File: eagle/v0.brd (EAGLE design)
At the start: 85.9 x 43.9 mm, 50 parts, among them IC1 MCP23008/SO, J12 455-1750-1-ND, J13 455-1750-1-ND, J14 455-1750-1-ND, J15 455-1750-1-ND, Q1 IRLML6244, Q2 IRLML6244, Q3 IRLML6244, Q4 IRLML6244, Q5 IRLML6244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

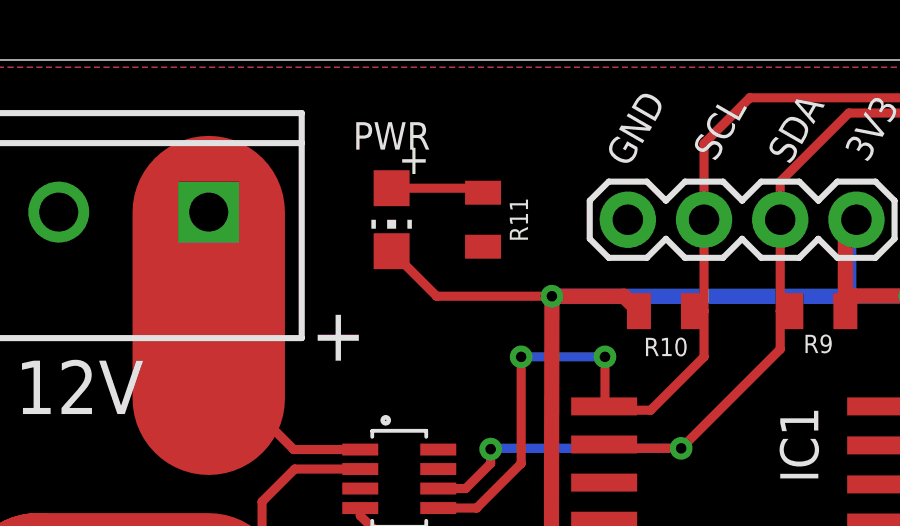
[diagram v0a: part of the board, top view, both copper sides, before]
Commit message: Fix LED polarity - caught by my dad :)
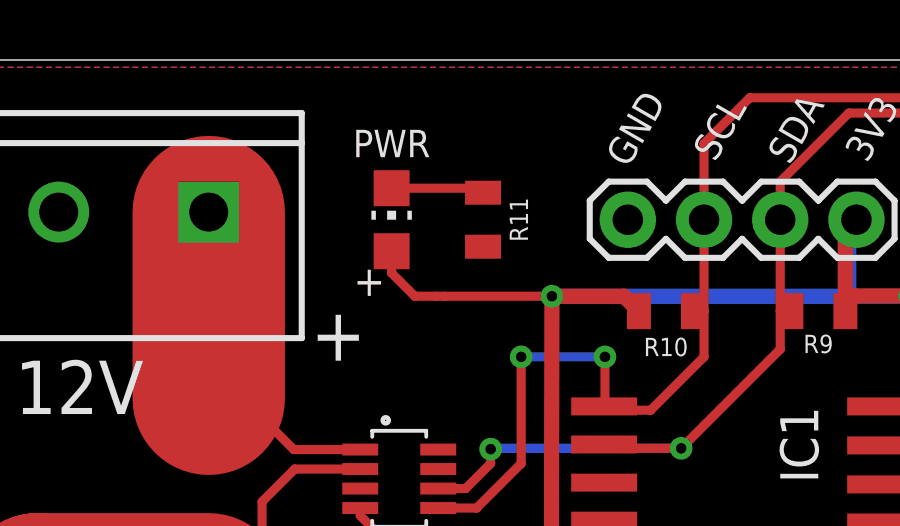
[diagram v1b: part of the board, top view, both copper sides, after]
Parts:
- turned PWR to 0 degrees
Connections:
- net N$17: now also PWR.C; no longer PWR.A
- net VCCIO: now also PWR.A; no longer PWR.C
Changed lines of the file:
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@@
 <drawing>
 <settings>
-<setting alwaysvectorfont="no"/>
+<setting alwaysvectorfont="yes"/>
 <setting verticaltext="up"/>
 </settings>
@@
 <attribute name="VALUE" x="74.93" y="6.35" size="0.6096" layer="27" font="vector" ratio="20"/>
 </element>
-<element name="PWR" library="adafruit" package="CHIP-LED0805" value="" x="16.256" y="38.608" smashed="yes" rot="R180">
-<attribute name="NAME" x="16.256" y="41.402" size="0.9144" layer="25" align="center"/>
-<attribute name="VALUE" x="13.716" y="39.878" size="1.27" layer="27" rot="R270"/>
+<element name="PWR" library="adafruit" package="CHIP-LED0805" value="" x="16.256" y="38.608" smashed="yes">
+<attribute name="NAME" x="16.256" y="41.148" size="0.9144" layer="25" rot="R180" align="center"/>
+<attribute name="VALUE" x="18.796" y="37.338" size="1.27" layer="27" rot="R90"/>
 </element>
 <element name="Q1" library="bytewerk-transistor" package="SOT23" value="IRLML6244" x="10.033" y="11.938" smashed="yes" rot="R180">
@@
 <contactref element="R10" pad="2"/>
 <contactref element="J10" pad="4"/>
-<contactref element="PWR" pad="C"/>
 <wire x1="31.38" y1="35.56" x2="31.38" y2="36.068" width="0.508" layer="1"/>
 <wire x1="31.38" y1="36.068" x2="31.38" y2="38.238" width="0.508" layer="1"/>
@@
 <wire x1="24.0024" y1="36.0576" x2="24.5" y2="35.56" width="0.508" layer="1"/>
 <wire x1="33.528" y1="36.068" x2="31.38" y2="36.068" width="0.508" layer="1"/>
-<wire x1="16.256" y1="37.558" x2="17.7564" y2="36.0576" width="0.3048" layer="1"/>
-<wire x1="17.7564" y1="36.0576" x2="21.6004" y2="36.0576" width="0.3048" layer="1"/>
+<wire x1="21.6004" y1="36.0576" x2="18.034" y2="36.0576" width="0.3048" layer="1"/>
 <contactref element="U1" pad="4"/>
+<wire x1="18.034" y1="36.0576" x2="17.7564" y2="36.0576" width="0.3048" layer="1"/>
 <wire x1="21.58564375" y1="20.31564375" x2="20.32" y2="19.05" width="0.508" layer="1"/>
 <wire x1="21.58564375" y1="20.31564375" x2="21.58564375" y2="25.908" width="0.508" layer="1"/>
@@
 <wire x1="31.75" y1="38.608" x2="31.496" y2="38.354" width="0.508" layer="16"/>
 <wire x1="31.496" y1="38.354" x2="31.496" y2="36.0576" width="0.508" layer="16"/>
+<contactref element="PWR" pad="A"/>
+<wire x1="17.7564" y1="36.0576" x2="17.0284" y2="36.0576" width="0.3048" layer="1"/>
+<wire x1="17.0284" y1="36.0576" x2="16.256" y2="36.83" width="0.3048" layer="1"/>
+<wire x1="16.256" y1="36.83" x2="16.256" y2="37.558" width="0.3048" layer="1"/>
 </signal>
 <signal name="SDA">
@@
 <via x="20.574" y="34.036" extent="1-16" drill="0.35"/>
 </signal>
-<signal name="N$17">
-<contactref element="PWR" pad="A"/>
-<contactref element="R11" pad="1"/>
-<wire x1="19.304" y1="39.508" x2="19.154" y2="39.658" width="0.3048" layer="1"/>
-<wire x1="19.154" y1="39.658" x2="16.256" y2="39.658" width="0.3048" layer="1"/>
-</signal>
 <signal name="RXD">
 <contactref element="MDL1" pad="15"/>
@@
 <wire x1="10.16" y1="38.862" x2="10.16" y2="32.639" width="5.08" layer="1"/>
 </signal>
+<signal name="N$17">
+<contactref element="R11" pad="1"/>
+<contactref element="PWR" pad="C"/>
+<wire x1="16.256" y1="39.658" x2="19.154" y2="39.658" width="0.3048" layer="1"/>
+<wire x1="19.154" y1="39.658" x2="19.304" y2="39.508" width="0.3048" layer="1"/>
+</signal>
 </signals>
